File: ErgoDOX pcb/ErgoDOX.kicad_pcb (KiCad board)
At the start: 2 copper layers, 182.8 x 158.9 mm, 61 parts, among them J1 USB, J2 3.5mm, J3 JMP, J4 JMP, SW0:10 SW0:3, SW0:11 SW0:2, SW0:12 SW0:1, SW0:7 SW0:6, SW0:8 SW0:5, SW0:9 SW0:4, SW1:10 SW1:3, SW1:11 SW1:2, SW1:12 SW1:1, SW1:13 SW1:0, SW1:9 SW1:4, SW2:10 SW2:3, SW2:11 SW2:2, SW2:12 SW2:1, SW2:13 SW2:0, SW2:7 SW2:6, SW2:8 SW2:5, SW2:9 SW2:4, SW3:10 SW3:3, SW3:11 SW3:2, SW3:12 SW3:1, SW3:13 SW3:0, SW3:8 SW3:5, SW3:9 SW3:4, SW4:10 SW4:3, SW4:11 SW4:2, SW4:12 SW4:1, SW4:13 SW4:0, SW4:7 SW4:6, SW4:8 SW4:5, SW4:9 SW4:4, SW5:10 SW5:3, SW5:11 SW5:2, SW5:12 SW5:1, SW5:13 SW5:0, SW5:7 SW5:6, SW5:8 SW5:5, SW5:9 SW5:4, U1 TEENSY2.0, U2 MCP23018

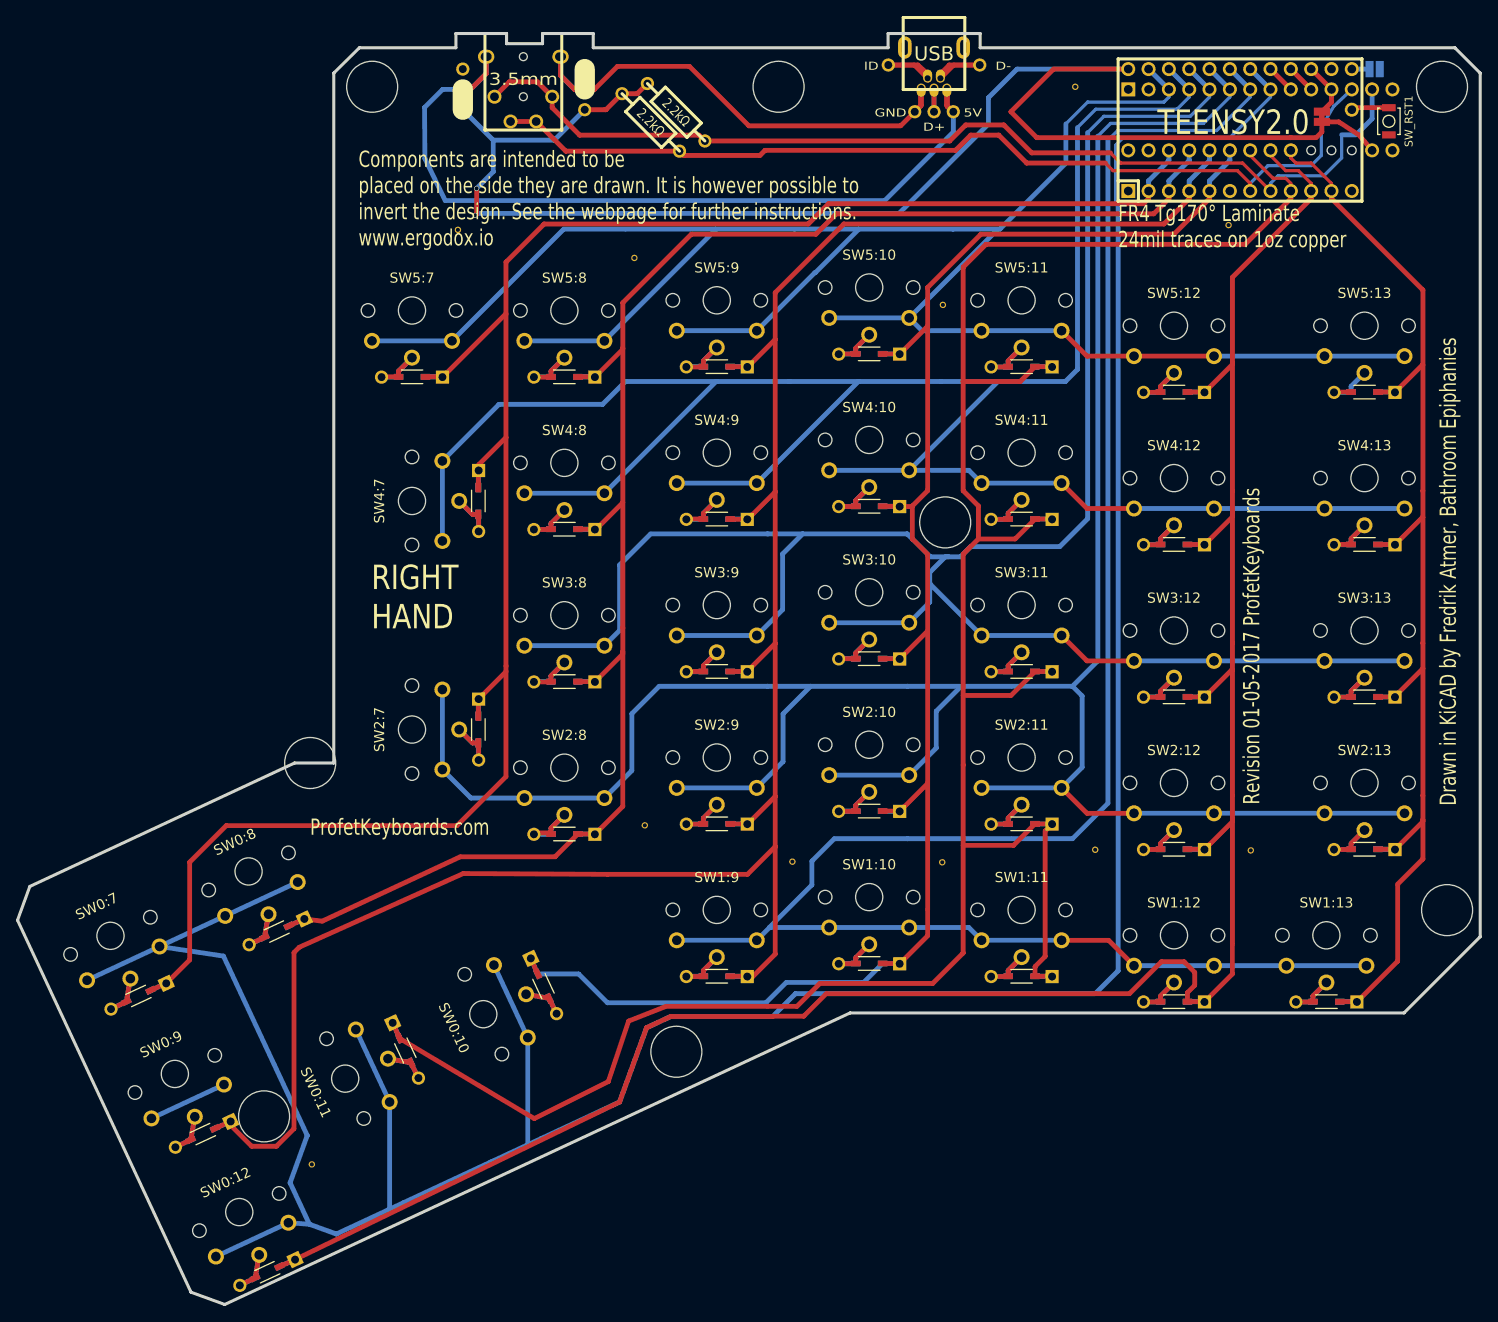
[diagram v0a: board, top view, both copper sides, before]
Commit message: change to usb c single side
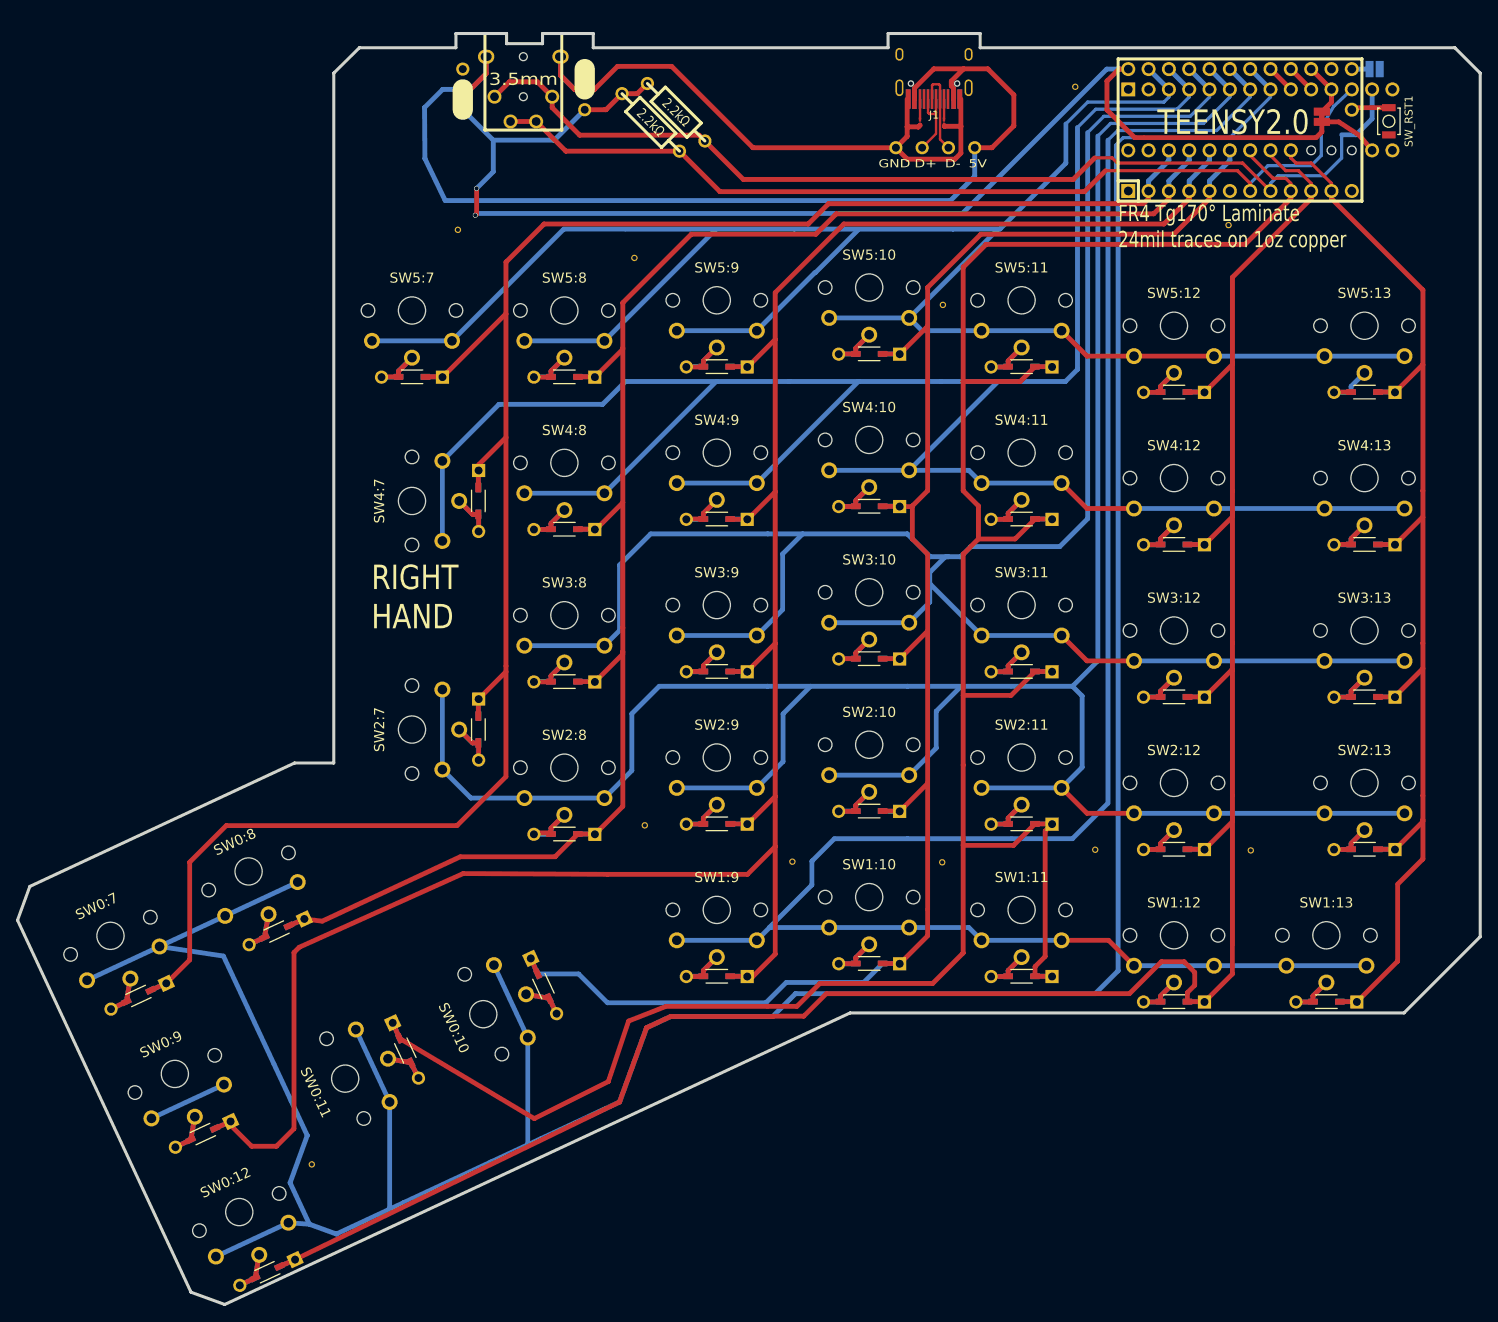
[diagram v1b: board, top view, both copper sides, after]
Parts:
- removed H99: MECHANICAL, ErgoDOXmech
- added REF**: R_01005_0402Metric_Pad0.57x0.30mm_HandSolder, Resistor_SMD:R_01005_0402Metric_Pad0.57x0.30mm_HandSolder, F.Cu at (135.9, 41.6)
- added REF**: R_01005_0402Metric_Pad0.57x0.30mm_HandSolder, Resistor_SMD:R_01005_0402Metric_Pad0.57x0.30mm_HandSolder, F.Cu at (138.9, 41.6)
- added STITCHING_VIA: ~, lib_footprints:STITCHING_VIA, F.Cu at (142.7, 44.8)
- added STITCHING_VIA: ~, lib_footprints:STITCHING_VIA, F.Cu at (139.4, 44.8)
- added STITCHING_VIA: ~, lib_footprints:STITCHING_VIA, F.Cu at (132.9, 44.8)
- added STITCHING_VIA: ~, lib_footprints:STITCHING_VIA, F.Cu at (136.2, 44.8)
- J1: footprint USBMINImod -> ErgoDOX pcb:HRO-TYPE-C-31-M-12-HandSoldering
- turned J1 to 180 degrees
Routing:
- net Net-(J1-Pad1): track 102.6 -> 131.3 mm
- net VCC: track 204.7 -> 180.9 mm
- net Net-(J1-Pad5): track 61.7 -> 82.7 mm
- net /Net-(J1-Pad3): track 2.98 -> 9.64 mm
- net /Net-(J1-Pad4): track 5.60 -> 0.00 mm
- net /Net-(J1-Pad2): track 5.60 -> 11.1 mm
- net /Net-(J1-CC2): track 0.00 -> 2.54 mm
- net /Net-(J1-CC1): track 0.00 -> 2.49 mm
- net /SDAM: track 128.3 -> 128.8 mm
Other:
- rule pad_to_mask_clearance: 0.2032 -> 0
- board text removed: "Components are intended to be placed on the side they are drawn. It is however possible to invert the design. See the webpage for further instructions. www.ergodox.io"
- board text removed: "Design by Dominic Beauchamp, based on the Key64 by Nestor A. Diaz"
- board text removed: "Drawn in KiCAD by Fredrik Atmer, Bathroom Epiphanies"
- board text removed: "ErgoDox"
- board text removed: "ID"
- board text removed: "ProfetKeyboards.com"
- board text removed: "Revision 01-05-2017 ProfetKeyboards"

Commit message: update with reroute to use nice nano v2 and choc hotswap footprint
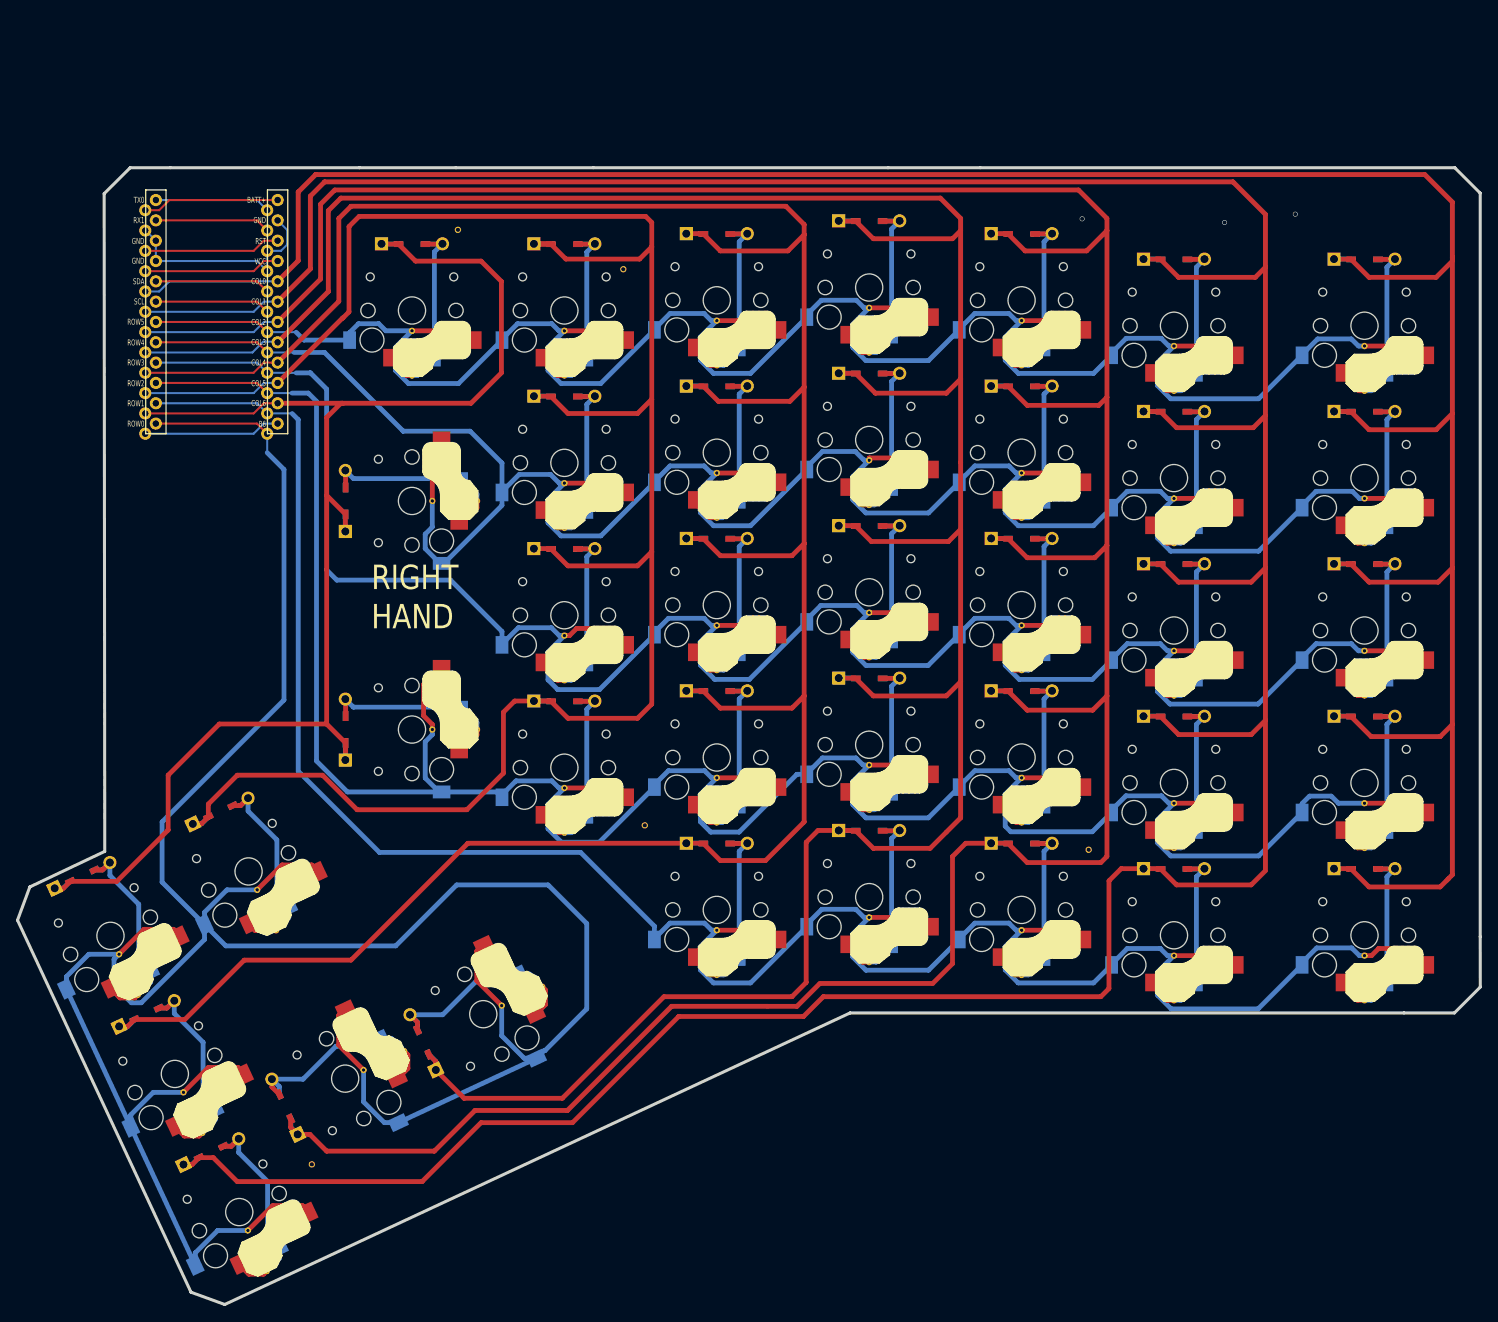
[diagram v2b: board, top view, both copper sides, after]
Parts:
- removed J1: USB, ErgoDOX pcb:HRO-TYPE-C-31-M-12-HandSoldering
- removed J2: 3.5mm, 4pin35mmAudio
- removed J3, J4: JMP, 100PITCH1X3
- removed JP1, JP2: JUMPER, GAP
- removed R1, R2: 2.2kΩ, RESISTOR
- removed REF** (x2): R_01005_0402Metric_Pad0.57x0.30mm_HandSolder, Resistor_SMD:R_01005_0402Metric_Pad0.57x0.30mm_HandSolder
- removed the STITCHING_VIA at (138.8, 64.4)
- removed the STITCHING_VIA at (177.2, 132.6)
- removed the STITCHING_VIA at (142.7, 44.8)
- removed the STITCHING_VIA at (139.4, 44.8)
- removed the STITCHING_VIA at (132.9, 44.8)
- removed the STITCHING_VIA at (136.2, 44.8)
- removed the STITCHING_VIA at (174.5, 54.4)
- removed the STITCHING_VIA at (155.3, 37.1)
- removed the STITCHING_VIA at (119.9, 134.0)
- removed the STITCHING_VIA at (138.7, 134.1)
- removed SW_RST1: SWITCH_PUSH, Buttons_Switches_SMD:SW_SPST_B3U-1000P
- removed U2: MCP23018, DIP28_300
- SW0:10, SW0:11, SW0:12, SW0:7, SW0:8, SW0:9, SW1:10, SW1:11, SW1:12, SW1:13, SW1:9, SW2:10, SW2:11, SW2:12, SW2:13, SW2:7, SW2:8, SW2:9, SW3:10, SW3:11, SW3:12, SW3:13, SW3:8, SW3:9, SW4:10, SW4:11, SW4:12, SW4:13, SW4:7, SW4:8, SW4:9, SW5:12, SW5:13, SW5:7, SW5:8, SW5:9: footprint ErgoDOX pcb:SW_choc_Reversible_1u -> ErgoDOX pcb:Choc_Hotswap
- SW5:10, SW5:11: footprint marbastlib:SW_choc_Reversible_1u -> ErgoDOX pcb:Choc_Hotswap
- U1: value TEENSY2.0 -> nice!nano; footprint ErgoDOX pcb:TEENSY_2.0_WITH_RESET -> ErgoDOX pcb:nicenano
- moved U1 130.1 mm to (47.9, 65.8)
- moved SW1:13 4.76 mm to (191.5, 143.2)
- moved STITCHING_VIA 1.98 mm to (98.8, 59.9)
- moved STITCHING_VIA 0.82 mm to (157.0, 132.5)
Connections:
- net /LED_C renamed NET-(U3-PAD6)
- U1 pad 1: GND -> NET-(U3-PAD1)
- U1 pad 10: /COL1 -> /ROW2
- U1 pad 11: /COL0 -> /ROW1
- U1 pad 12: /Net-(U1-Pad12) -> /ROW0
- U1 pad 16: /RST -> /COL4
- U1 pad 18: GND -> /COL11
- U1 pad 19: /Net-(U1-Pad19) -> /COL1
- U1 pad 2: /COL6 -> NET-(U3-PAD2)
- U1 pad 20: VCC -> /COL0
- U1 pad 21: /LED_A -> VCC
- U1 pad 22: /LED_B -> /RST
- U1 pad 23: /ROW0 -> GND
- U1 pad 24: /ROW1 -> +BATT
- U1 pad 3: /COL5 -> GND
- U1 pad 4: /COL4 -> GND
- U1 pad 5: /COL10 -> NET-(U3-PAD5)
- U1 pad 7: /SCLM -> /ROW5
- U1 pad 8: /SDAM -> /ROW4
- U1 pad 9: /COL11 -> /ROW3
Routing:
- net /COL0: track 158.7 -> 353.2 mm
- net /COL1: track 291.6 -> 478.1 mm
- net VCC: track 180.9 -> 17.1 mm, vias 2 -> 0
- net /COL10: track 222.7 -> 367.5 mm
- net Net-(J1-Pad1): track 131.3 -> 0.00 mm
- net /SDAM: track 128.8 -> 0.00 mm
- net /SCLM: track 119.7 -> 0.00 mm
- net /COL11: track 306.4 -> 420.9 mm
- net Net-(J1-Pad5): track 82.7 -> 0.00 mm
- net /COL6: track 253.7 -> 182.0 mm
- net /COL4: track 291.6 -> 348.5 mm
- net /COL5: track 221.8 -> 275.0 mm
- net /ROW1: track 246.8 -> 298.9 mm
- net /ROW0: track 387.4 -> 348.9 mm
- net /ROW3: track 263.0 -> 295.5 mm
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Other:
- board size 182.8 x 158.9 mm -> 182.8 x 142.1 mm
- board text removed: "5V"
- board text removed: "D+"
- board text removed: "D-"
- board text removed: "FR4 Tg170° Laminate 24mil traces on 1oz copper"
- board text removed: "GND"

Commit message: good for prod
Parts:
- added BATTERY: Battery_Wire_Connector, ErgoDOX pcb:Battery_Wire_Connector, F.Cu at (38.7, 97.2)
- added BSW1: SW_DPDT_x2, ErgoDOX pcb:SS-12D00, F.Cu at (38.7, 90.9)
- added RSW1: SW_Push, ErgoDOX pcb:ResetSW, F.Cu at (49.2, 88.3)
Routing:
- net /RST: track 17.1 -> 62.4 mm
- net +BATT: track 17.1 -> 52.6 mm
- net NET-(BSW1-PAD2): track 0.00 -> 10.2 mm
